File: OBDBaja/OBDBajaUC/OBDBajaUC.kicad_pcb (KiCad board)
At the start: 2 copper layers, 36.2 x 58.4 mm, 12 parts, among them J1 Conn_01x01, J2 Conn_01x02, J3 Conn_01x10, J4 Conn_01x01, J5 Conn_01x14, J6 Conn_01x01, U1 Teensy4.0

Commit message: Updated OBD Baja file organization
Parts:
- J1, J4, J6: footprint Connector_PinHeader_2.54mm:PinHeader_1x01_P2.54mm_Vertical -> Connector_PinHeader_2.54mm:PinHeader_1x01_P2.54mm_Horizontal
- J2: footprint Connector_PinHeader_2.54mm:PinHeader_1x02_P2.54mm_Vertical -> Connector_PinHeader_2.54mm:PinHeader_1x02_P2.54mm_Horizontal
- J5: footprint Connector_PinHeader_2.54mm:PinHeader_1x14_P2.54mm_Vertical -> Connector_PinSocket_2.54mm:PinSocket_1x14_P2.54mm_Vertical

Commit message: Finished PCB and test enclosure
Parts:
- added J7: Conn_01x06, Connector_PinHeader_2.54mm:PinHeader_1x06_P2.54mm_Horizontal, F.Cu at (170.8, 95.0)
- added MH3: MountingHole_3.2mm_M3, MountingHole:MountingHole_3.2mm_M3, F.Cu at (179.7, 50.2)
- added MH4: MountingHole_3.2mm_M3, MountingHole:MountingHole_3.2mm_M3, F.Cu at (179.7, 101.0)
- moved MH1 28.6 mm to (151.1, 50.2)
- moved MH2 28.6 mm to (151.1, 101.0)
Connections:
- U1 pad 26: unconnected-(U1-19_A5_SCL0-Pad26) -> /UP
- U1 pad 27: unconnected-(U1-20_A6_TX5_LRCLK1-Pad27) -> /DN
- U1 pad 28: unconnected-(U1-21_A7_RX5_BCLK1-Pad28) -> /L
- U1 pad 29: unconnected-(U1-22_A8_CTX1-Pad29) -> /R
- U1 pad 30: unconnected-(U1-23_A9_CRX1_MCLK1-Pad30) -> /SEL
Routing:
- net /SEL: track 0.00 -> 41.3 mm
- net /R: track 0.00 -> 36.3 mm, vias 0 -> 1
- net /L: track 0.00 -> 34.6 mm, vias 0 -> 1
- net /UP: track 0.00 -> 28.6 mm, vias 0 -> 1
- net /DN: track 0.00 -> 27.9 mm, vias 0 -> 1
- net /T_IRQ: track 47.2 -> 47.7 mm, vias 0 -> 2
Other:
- outline, holes or cut-outs redrawn
- board text added: "3.3V"

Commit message: Added images
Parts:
- C1: value C -> .1uF
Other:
- board text added: "JLCJLCJLCJLC"
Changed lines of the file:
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@@
       (plot_on_all_layers_selection 0x0000000_00000000)
       (disableapertmacros false)
-      (usegerberextensions false)
+      (usegerberextensions true)
       (usegerberattributes true)
       (usegerberadvancedattributes true)
@@
       (plotinvisibletext false)
       (sketchpadsonfab false)
-      (subtractmaskfromsilk false)
+      (subtractmaskfromsilk true)
       (outputformat 1)
       (mirror false)
-      (drillshape 1)
+      (drillshape 0)
       (scaleselection 1)
       (outputdirectory "")
@@
         (effects (font (size 1 1) (thickness 0.15)))
     )
-    (fp_text value "C" (at 0 1.68 90) (layer "F.Fab")
+    (fp_text value ".1uF" (at 0 1.68 90) (layer "F.Fab")
         (effects (font (size 1 1) (thickness 0.15)))
     )
@@
     (fp_line (start 1 0.625) (end -1 0.625)
       (stroke (width 0.1) (type solid)) (layer "F.Fab"))
-    (pad "1" smd roundrect (at -1.0375 0 90) (size 1.175 1.45) (layers "F.Cu" "F.Paste" "F.Mask") (roundrect_rratio 0.212766)
+    (pad "1" smd roundrect (at -1.0375 0 90) (size 1.175 1.45) (layers "F.Cu" "F.Paste" "F.Mask") (roundrect_rratio 0.2127659574)
       (net 1 "GND") (pintype "passive"))
-    (pad "2" smd roundrect (at 1.0375 0 90) (size 1.175 1.45) (layers "F.Cu" "F.Paste" "F.Mask") (roundrect_rratio 0.212766)
+    (pad "2" smd roundrect (at 1.0375 0 90) (size 1.175 1.45) (layers "F.Cu" "F.Paste" "F.Mask") (roundrect_rratio 0.2127659574)
       (net 2 "+5V") (pintype "passive"))
     (model "${KICAD6_3DMODEL_DIR}/Capacitor_SMD.3dshapes/C_0805_2012Metric.wrl"
@@
     (fp_line (start 1 0.625) (end -1 0.625)
       (stroke (width 0.1) (type solid)) (layer "F.Fab"))
-    (pad "1" smd roundrect (at -1 0 270) (size 1.2 1.4) (layers "F.Cu" "F.Paste" "F.Mask") (roundrect_rratio 0.208333)
+    (pad "1" smd roundrect (at -1 0 270) (size 1.2 1.4) (layers "F.Cu" "F.Paste" "F.Mask") (roundrect_rratio 0.2083333333)
       (net 2 "+5V") (pintype "passive"))
-    (pad "2" smd roundrect (at 1 0 270) (size 1.2 1.4) (layers "F.Cu" "F.Paste" "F.Mask") (roundrect_rratio 0.208333)
+    (pad "2" smd roundrect (at 1 0 270) (size 1.2 1.4) (layers "F.Cu" "F.Paste" "F.Mask") (roundrect_rratio 0.2083333333)
       (net 43 "Net-(J5-Pin_8)") (pintype "passive"))
     (model "${KICAD6_3DMODEL_DIR}/Resistor_SMD.3dshapes/R_0805_2012Metric.wrl"
@@
   (gr_arc (start 154.94 100.965) (mid 151.13 104.775) (end 147.32 100.965)
     (stroke (width 0.1) (type default)) (layer "Edge.Cuts"))
+  (gr_text "JLCJLCJLCJLC" (at 182.499 92.837 90) (layer "B.SilkS")
+    (effects (font (size 0.889 0.889) (thickness 0.127)) (justify mirror))
+  )
   (gr_text "D6" (at 177.8 76.708) (layer "F.SilkS")
     (effects (font (size 1 1) (thickness 0.15)) (justify right))

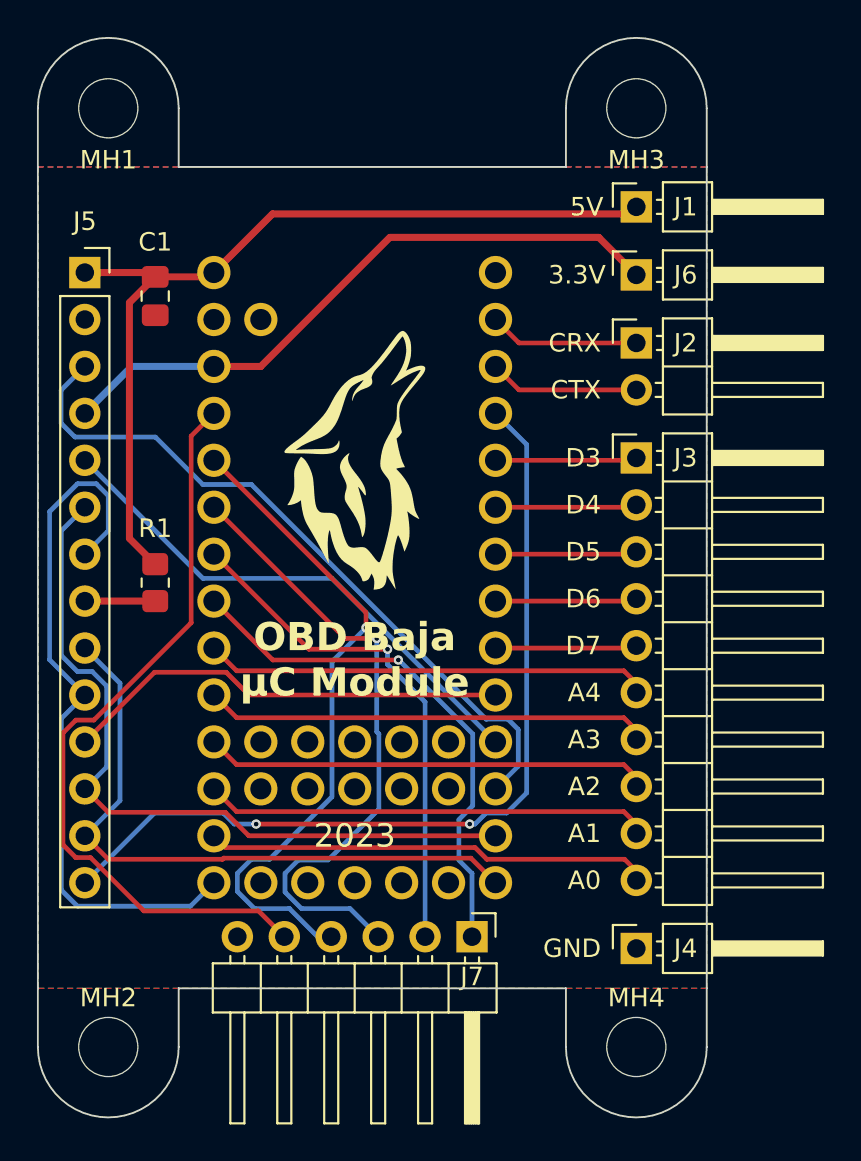
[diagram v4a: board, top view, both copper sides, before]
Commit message: Updated to UC V1.1
Fixed screen connector and teensy holes
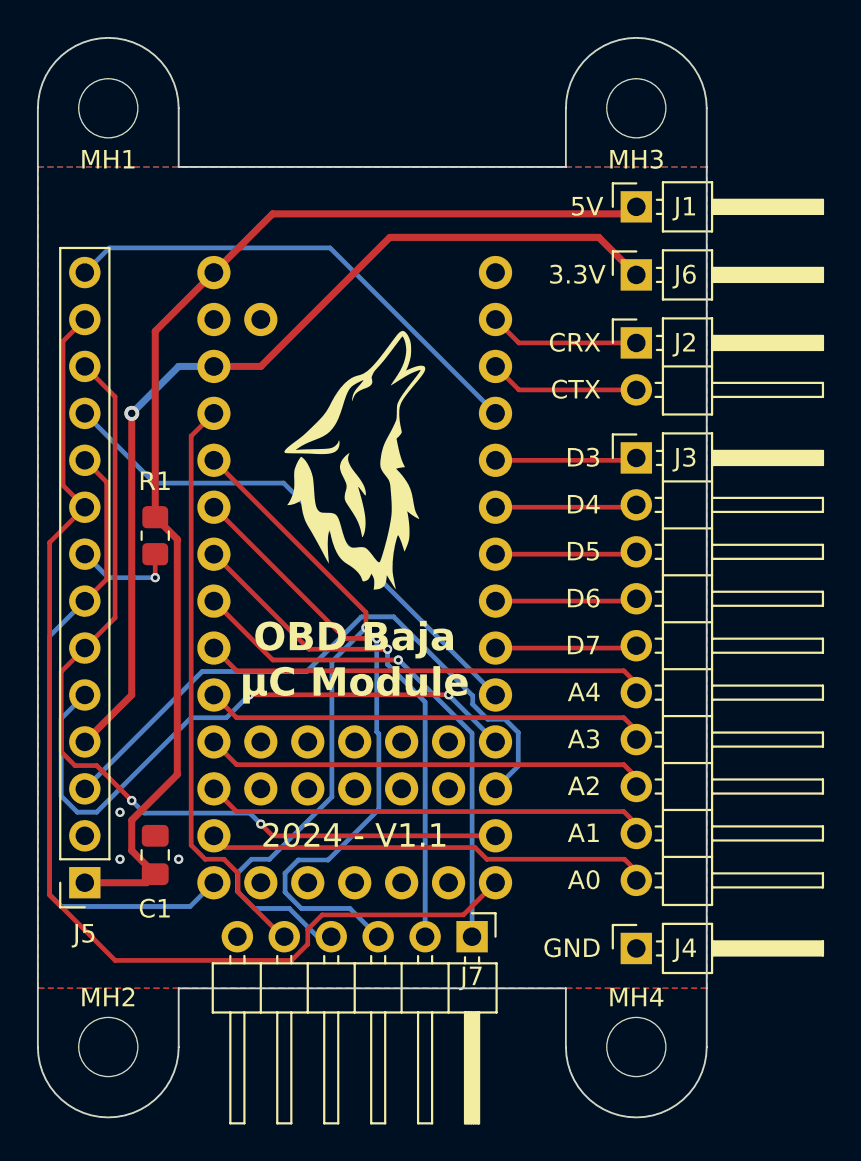
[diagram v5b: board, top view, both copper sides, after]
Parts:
- moved J5 33.0 mm to (149.9, 92.1), turned to 180 degrees
- moved C1 30.2 mm to (153.7, 90.6), turned to -90 degrees
- moved R1 2.54 mm to (153.7, 73.3)
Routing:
- net /SDO: track 35.1 -> 60.7 mm
- net /T_IRQ: track 47.7 -> 26.5 mm, vias 2 -> 0
- net +3.3V: track 34.6 -> 50.9 mm, vias 0 -> 1
- net +5V: track 48.1 -> 64.1 mm
- net /SEL: track 41.3 -> 31.6 mm
- net /SDI: track 41.0 -> 48.1 mm, vias 0 -> 2
- net /CS: track 38.9 -> 33.7 mm
- net /DC: track 28.5 -> 33.6 mm, vias 0 -> 2
- net /T_CS: track 24.3 -> 28.5 mm
- net /SCK: track 38.7 -> 35.0 mm
- net Net-(J5-Pin_8): track 3.81 -> 5.61 mm, vias 0 -> 1
- net /UP: track 28.6 -> 27.9 mm
- net GND: vias 0 -> 3
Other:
- board text added: "2024 - V1.1"
- board text removed: "2023"
